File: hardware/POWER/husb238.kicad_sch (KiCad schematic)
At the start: 8 parts, among them U1 HUSB238, U3 CSD25402Q3A

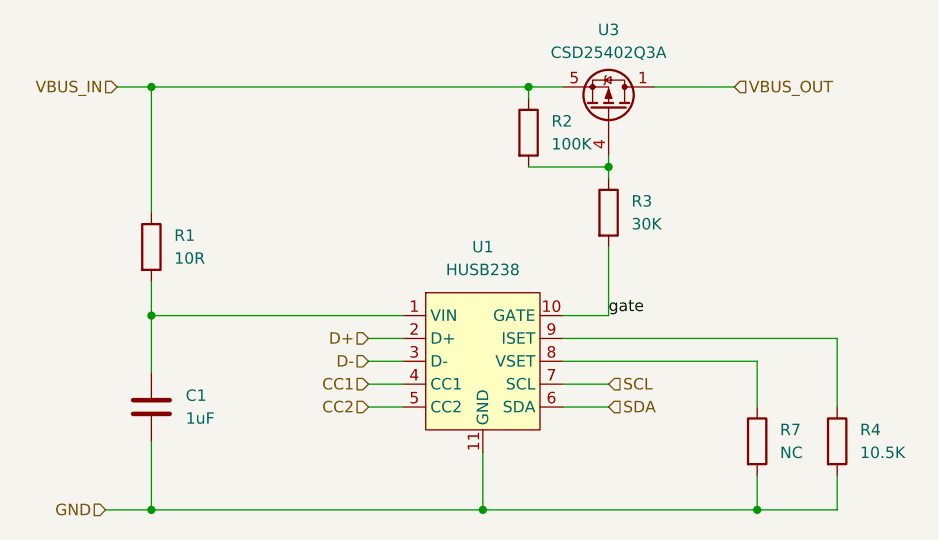
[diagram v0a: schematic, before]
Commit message: 硬件v1调整布局将肖特基二极管放置正面，便于贴片
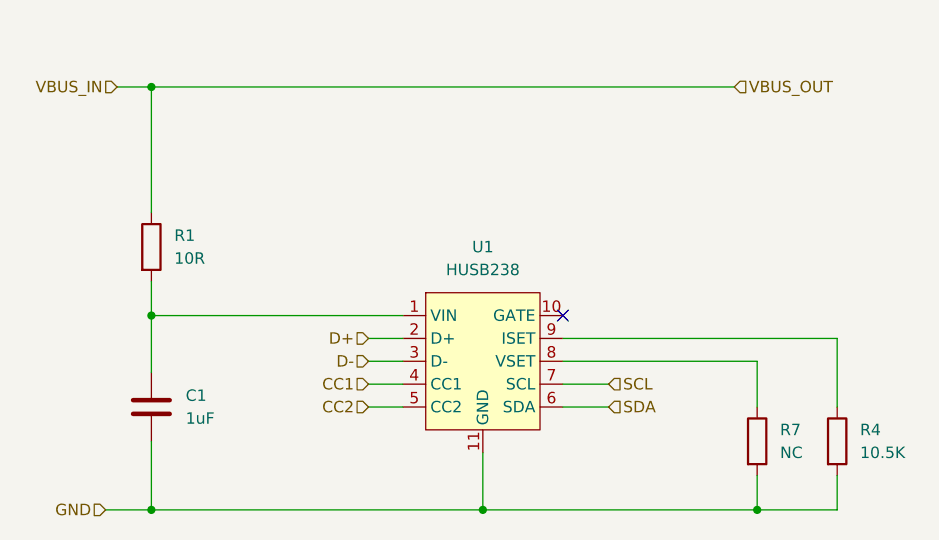
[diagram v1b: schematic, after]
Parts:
- removed R2: 100K, Resistor_SMD:R_0603_1608Metric, symbol Device:R
- removed R3: 30K, Resistor_SMD:R_0603_1608Metric, symbol Device:R
- removed U3: CSD25402Q3A, Package_SON:VSON-8_3.3x3.3mm_P0.65mm_NexFET, symbol Transistor_FET:CSD25402Q3A
- C1: footprint Capacitor_SMD:C_0402_1005Metric -> Capacitor_SMD:C_0603_1608Metric
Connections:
- net gate: no longer names the net of U1.10 (GATE)
- no-connect marks 0 -> 1

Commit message: 更换升压方案为同步整流，较大降低了升压电路的发热量，将acc和ldo放在电源板上
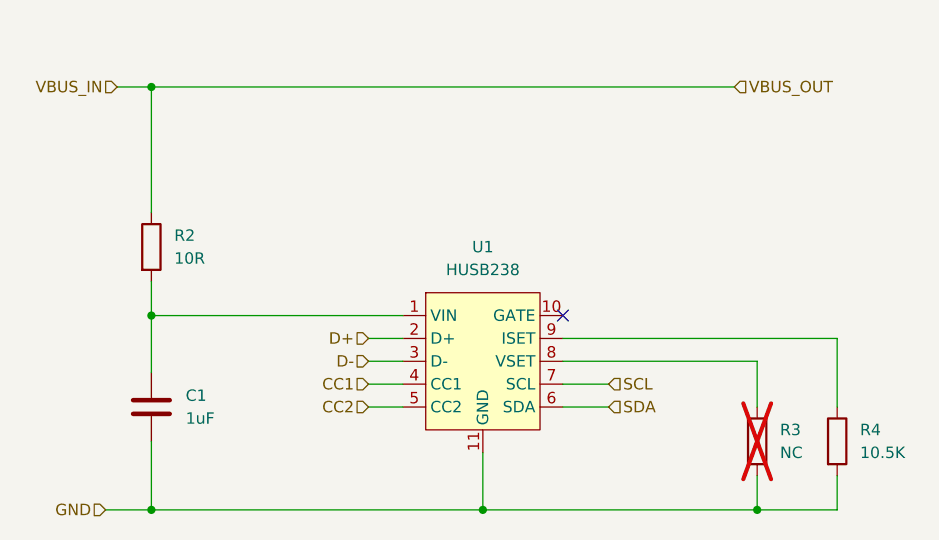
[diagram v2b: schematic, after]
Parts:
- C1: footprint Capacitor_SMD:C_0603_1608Metric -> Capacitor_SMD:C_0402_1005Metric
- R2: renamed from R1; footprint Resistor_SMD:R_0603_1608Metric -> Resistor_SMD:R_0402_1005Metric
- R3: renamed from R7; now not fitted; now left out of the parts list
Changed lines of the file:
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@@
 			)
 		)
-		(property "Footprint" "Capacitor_SMD:C_0603_1608Metric"
+		(property "Footprint" "Capacitor_SMD:C_0402_1005Metric"
 			(at 102.5652 106.68 0)
 			(effects
@@
 		(dnp no)
 		(fields_autoplaced yes)
-		(property "Reference" "R1"
+		(property "Reference" "R2"
 			(at 104.14 83.8199 0)
 			(effects
@@
 			)
 		)
-		(property "Footprint" "Resistor_SMD:R_0603_1608Metric"
+		(property "Footprint" "Resistor_SMD:R_0402_1005Metric"
 			(at 99.822 85.09 90)
 			(effects
@@
 			(project "PD24"
 				(path "/10096dd5-e34a-417b-937d-8bf7da4f4410/57b1b606-b677-42d1-83e9-4545144c6d1c"
-					(reference "R1")
+					(reference "R2")
 					(unit 1)
 				)
@@
 		(unit 1)
 		(exclude_from_sim no)
-		(in_bom yes)
-		(on_board yes)
-		(dnp no)
+		(in_bom no)
+		(on_board no)
+		(dnp yes)
 		(fields_autoplaced yes)
-		(property "Reference" "R7"
+		(property "Reference" "R3"
 			(at 171.45 105.4099 0)
 			(effects
@@
 			(project "PD24"
 				(path "/10096dd5-e34a-417b-937d-8bf7da4f4410/57b1b606-b677-42d1-83e9-4545144c6d1c"
-					(reference "R7")
-					(unit 1)
-				)
+					(reference "R3")
+					(unit 1)
+				)
